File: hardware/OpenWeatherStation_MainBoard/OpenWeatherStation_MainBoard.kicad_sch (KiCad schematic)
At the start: 2 parts

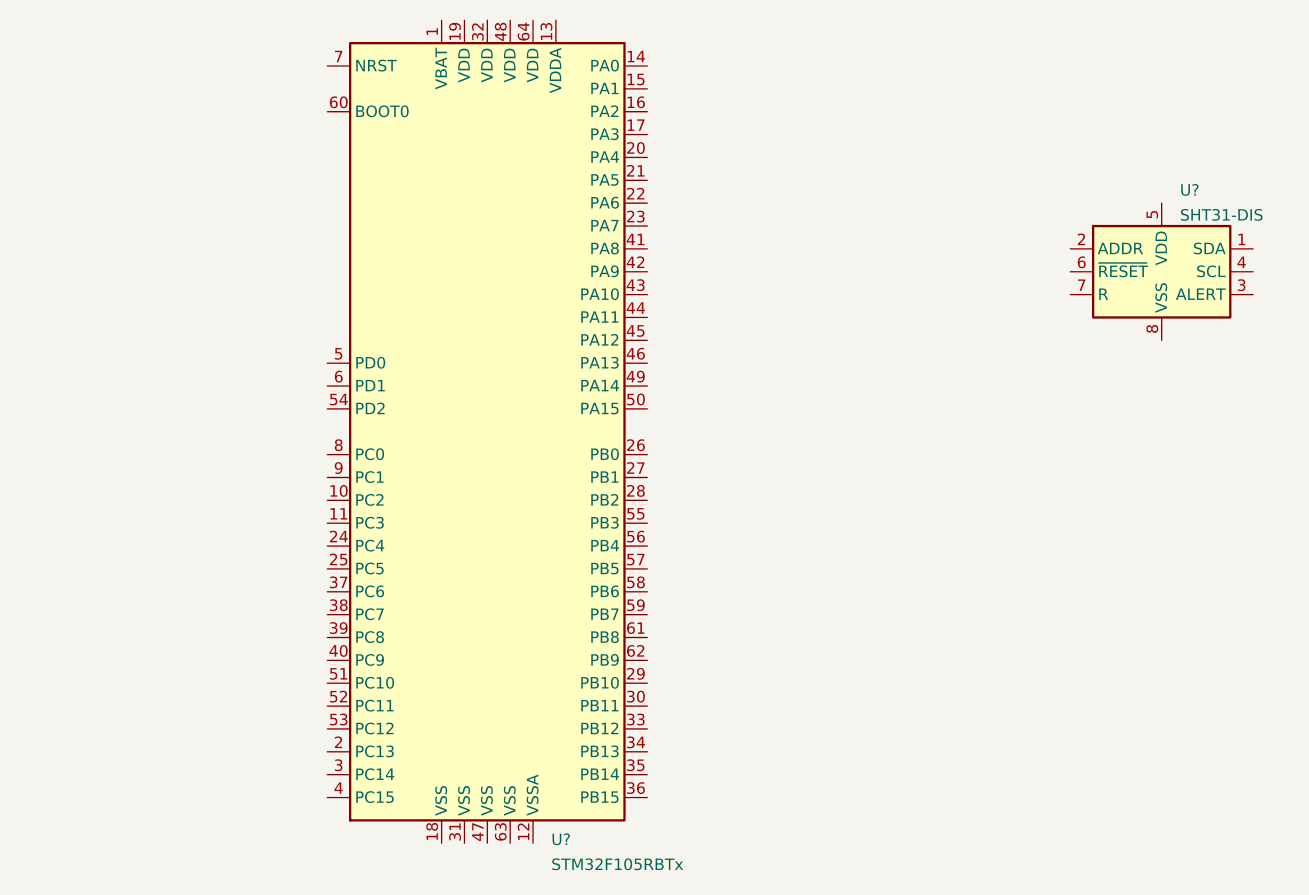
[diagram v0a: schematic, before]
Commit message: update schematic
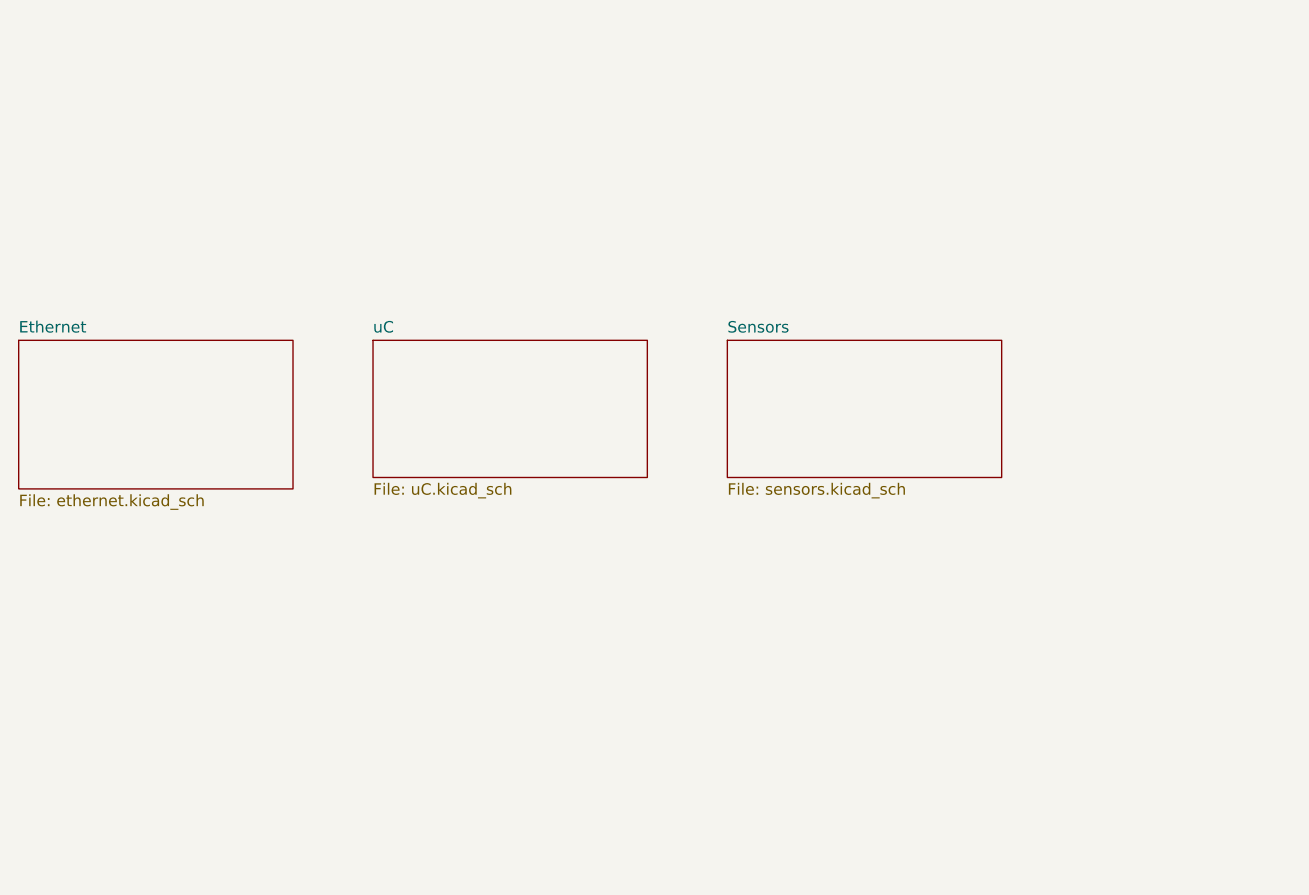
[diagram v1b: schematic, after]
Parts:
- removed U?: STM32F105RBTx, Package_QFP:LQFP-64_10x10mm_P0.5mm, symbol MCU_ST_STM32F1:STM32F105RBTx
- removed U?: SHT31-DIS, Sensor_Humidity:Sensirion_DFN-8-1EP_2.5x2.5mm_P0.5mm_EP1.1x1.7mm, symbol Sensor_Humidity:SHT31-DIS
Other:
- added sheet Ethernet (ethernet.kicad_sch)
- added sheet Sensors (sensors.kicad_sch)
- added sheet uC (uC.kicad_sch)
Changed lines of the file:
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@@
 (kicad_sch (version 20211123) (generator eeschema)
   (paper "A4")
-  (symbol (lib_id "MCU_ST_STM32F1:STM32F105RBTx") (at 140.97 88.9 0) (unit 1)
-    (in_bom yes) (on_board yes) (fields_autoplaced)
-    (property "Reference" "U?" (id 0) (at 148.0694 134.2295 0)
-      (effects (font (size 1.27 1.27)) (justify left))
+  (sheet (at 88.9 78.74) (size 30.48 16.51) (fields_autoplaced)
+    (stroke (width 0.1524) (type solid) (color 0 0 0 0))
+    (fill (color 0 0 0 0.0000))
+    (property "Sheet name" "Ethernet" (id 0) (at 88.9 78.0284 0)
+      (effects (font (size 1.27 1.27)) (justify left bottom))
     )
-    (property "Value" "STM32F105RBTx" (id 1) (at 148.0694 137.0046 0)
-      (effects (font (size 1.27 1.27)) (justify left))
+    (property "Sheet file" "ethernet.kicad_sch" (id 1) (at 88.9 95.8346 0)
+      (effects (font (size 1.27 1.27)) (justify left top))
     )
-    (property "Footprint" "Package_QFP:LQFP-64_10x10mm_P0.5mm" (id 2) (at 125.73 132.08 0)
-      (effects (font (size 1.27 1.27)) (justify right) hide)
+  )
+  (sheet (at 128.27 78.74) (size 30.48 15.24) (fields_autoplaced)
+    (stroke (width 0.1524) (type solid) (color 0 0 0 0))
+    (fill (color 0 0 0 0.0000))
+    (property "Sheet name" "uC" (id 0) (at 128.27 78.0284 0)
+      (effects (font (size 1.27 1.27)) (justify left bottom))
     )
-    (property "Datasheet" "http://www.st.com/st-web-ui/static/active/en/resource/technical/document/datasheet/CD00220364.pdf" (id 3) (at 140.97 88.9 0)
-      (effects (font (size 1.27 1.27)) hide)
+    (property "Sheet file" "uC.kicad_sch" (id 1) (at 128.27 94.5646 0)
+      (effects (font (size 1.27 1.27)) (justify left top))
     )
-    (pin "1")
-    (pin "10")
-    (pin "11")
-    (pin "12")
-    (pin "13")
-    (pin "14")
-    (pin "15")
-    (pin "16")
-    (pin "17")
-    (pin "18")
-    (pin "19")
-    (pin "2")
-    (pin "20")
-    (pin "21")
-    (pin "22")
-    (pin "23")
-    (pin "24")
-    (pin "25")
-    (pin "26")
-    (pin "27")
-    (pin "28")
-    (pin "29")
-    (pin "3")
-    (pin "30")
-    (pin "31")
-    (pin "32")
-    (pin "33")
-    (pin "34")
-    (pin "35")
-    (pin "36")
-    (pin "37")
-    (pin "38")
-    (pin "39")
-    (pin "4")
-    (pin "40")
-    (pin "41")
-    (pin "42")
-    (pin "43")
-    (pin "44")
-    (pin "45")
-    (pin "46")
-    (pin "47")
-    (pin "48")
-    (pin "49")
-    (pin "5")
-    (pin "50")
-    (pin "51")
-    (pin "52")
-    (pin "53")
-    (pin "54")
-    (pin "55")
-    (pin "56")
-    (pin "57")
-    (pin "58")
-    (pin "59")
-    (pin "6")
-    (pin "60")
-    (pin "61")
-    (pin "62")
-    (pin "63")
-    (pin "64")
-    (pin "7")
-    (pin "8")
-    (pin "9")
   )
-  (symbol (lib_id "Sensor_Humidity:SHT31-DIS") (at 215.9 71.12 0) (unit 1)
-    (in_bom yes) (on_board yes) (fields_autoplaced)
-    (property "Reference" "U?" (id 0) (at 217.9194 62.0735 0)
-      (effects (font (size 1.27 1.27)) (justify left))
+  (sheet (at 167.64 78.74) (size 30.48 15.24) (fields_autoplaced)
+    (stroke (width 0.1524) (type solid) (color 0 0 0 0))
+    (fill (color 0 0 0 0.0000))
+    (property "Sheet name" "Sensors" (id 0) (at 167.64 78.0284 0)
+      (effects (font (size 1.27 1.27)) (justify left bottom))
     )
-    (property "Value" "SHT31-DIS" (id 1) (at 217.9194 64.8486 0)
-      (effects (font (size 1.27 1.27)) (justify left))
+    (property "Sheet file" "sensors.kicad_sch" (id 1) (at 167.64 94.5646 0)
+      (effects (font (size 1.27 1.27)) (justify left top))
     )
-    (property "Footprint" "Sensor_Humidity:Sensirion_DFN-8-1EP_2.5x2.5mm_P0.5mm_EP1.1x1.7mm" (id 2) (at 215.9 69.85 0)
-      (effects (font (size 1.27 1.27)) hide)
-    )
-    (property "Datasheet" "https://www.sensirion.com/fileadmin/user_upload/customers/sensirion/Dokumente/2_Humidity_Sensors/Datasheets/Sensirion_Humidity_Sensors_SHT3x_Datasheet_digital.pdf" (id 3) (at 215.9 69.85 0)
-      (effects (font (size 1.27 1.27)) hide)
-    )
-    (pin "1")
-    (pin "2")
-    (pin "3")
-    (pin "4")
-    (pin "5")
-    (pin "6")
-    (pin "7")
-    (pin "8")
-    (pin "9")
   )
   (sheet_instances
     (path "/" (page "1"))
+    (path "/9484d3b4-a103-4051-8524-bb228ed28064" (page "3"))
+    (path "/aa496bd6-f95f-40ea-b623-d551df69cee4" (page "3"))
+    (path "/f004a257-e244-4519-8701-8e6b82831045" (page "5"))
   )
   (symbol_instances
-    (path "/0520f61d-4522-4301-a3fa-8ed0bf060f69"
-      (reference "U?") (unit 1) (value "STM32F105RBTx") (footprint "Package_QFP:LQFP-64_10x10mm_P0.5mm")
+    (path "/9484d3b4-a103-4051-8524-bb228ed28064/2e25a0d9-10d7-425a-a0fa-9a6a0352bed5"
+      (reference "U?") (unit 1) (value "USBLC6-4SC6") (footprint "Package_TO_SOT_SMD:SOT-23-6")
     )
-    (path "/3745d030-b1db-42b3-88e5-5fb982cc9164"
+    (path "/aa496bd6-f95f-40ea-b623-d551df69cee4/a36b1fb3-e4c2-43e2-ac73-12b7e7d1904b"
+      (reference "U?") (unit 1) (value "STM32F107VCTx") (footprint "Package_QFP:LQFP-100_14x14mm_P0.5mm")
+    )
+    (path "/f004a257-e244-4519-8701-8e6b82831045/b608c096-023e-4538-bb6b-d50ad5783720"
       (reference "U?") (unit 1) (value "SHT31-DIS") (footprint "Sensor_Humidity:Sensirion_DFN-8-1EP_2.5x2.5mm_P0.5mm_EP1.1x1.7mm")
     )
